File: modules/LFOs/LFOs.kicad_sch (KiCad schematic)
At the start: 12 parts, among them J1 BUS CONNECTOR, J10 LFO3 TRI, J2 LFO1 RMP, J3 LFO1 SQR, J4 LFO1 TRI, J5 LFO2 RMP, J6 LFO2 SQR, J7 LFO2 TRI, J8 LFO3 SAW, J9 LFO3 RMP

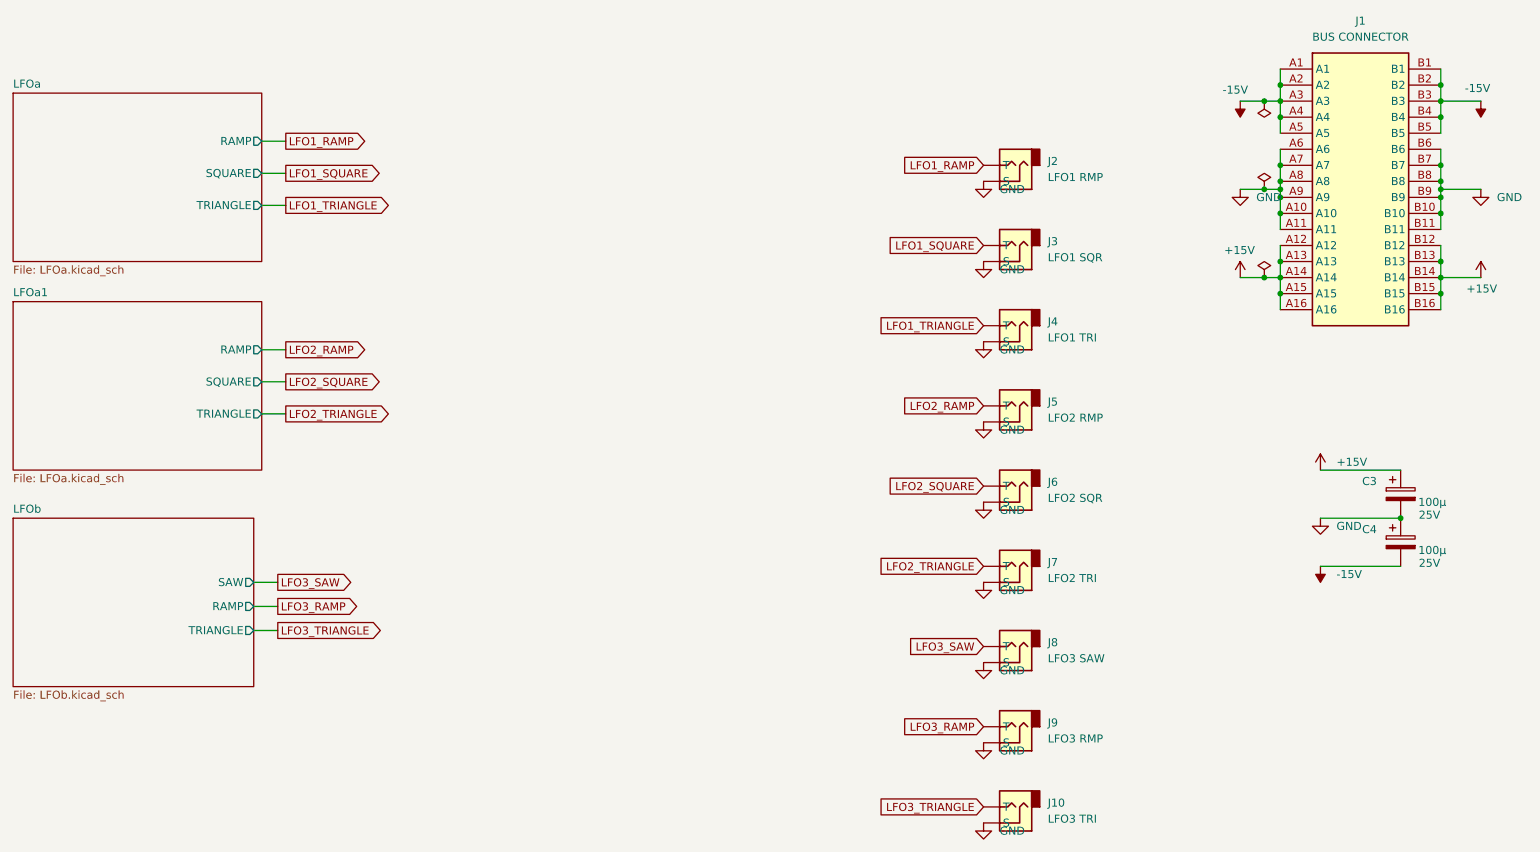
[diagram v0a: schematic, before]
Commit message: lfos overhaul to current template
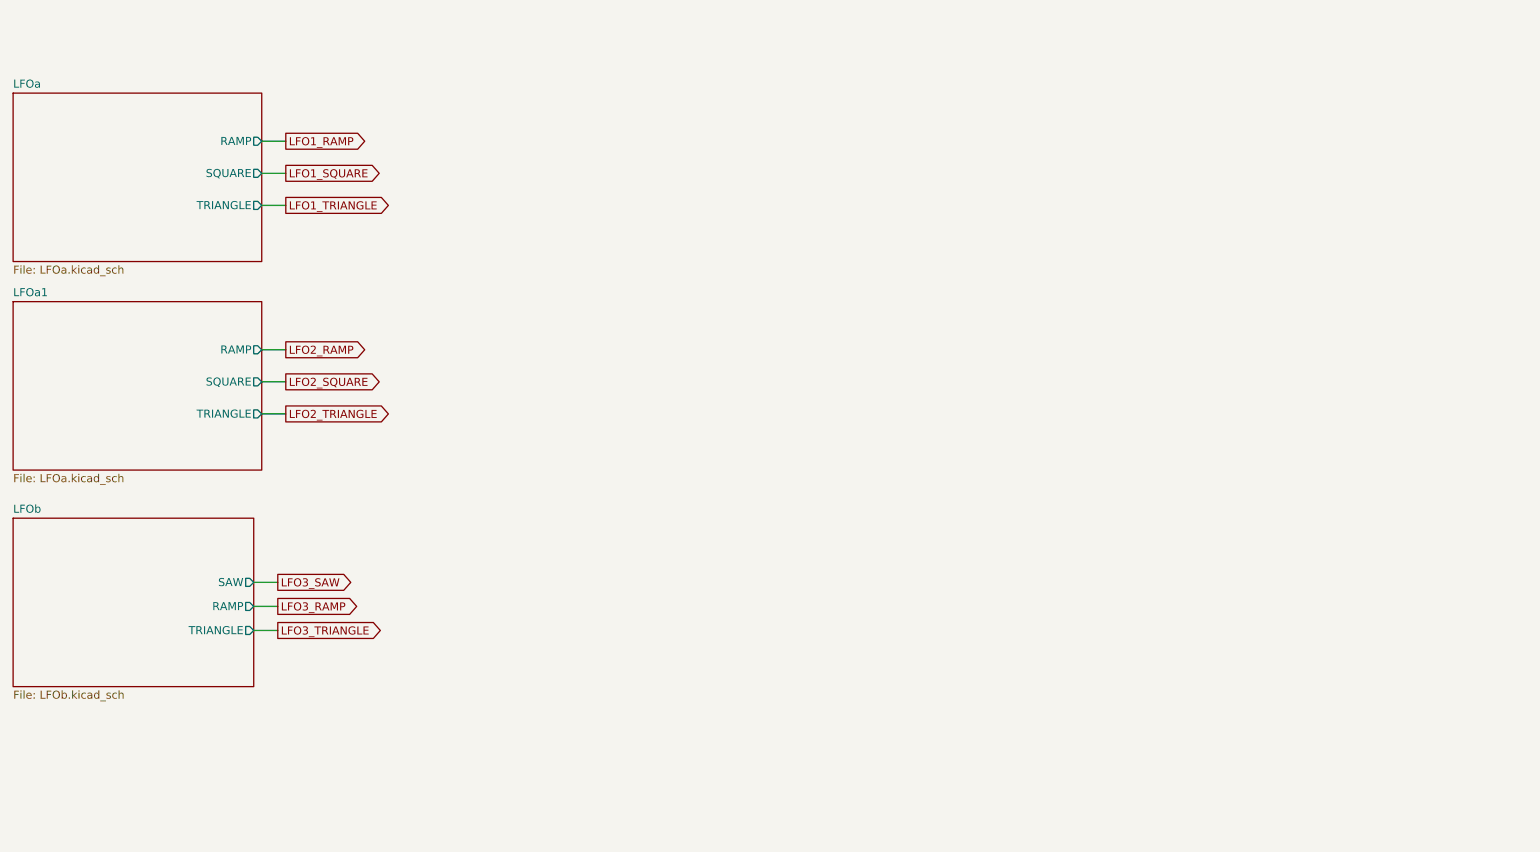
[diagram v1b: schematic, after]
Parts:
- removed C3, C4: 100µ, FormantKO:CP_Axial_800, symbol FormantKO:C_Polarized
- removed J1: BUS CONNECTOR, FormantKO:DIN_Male, symbol FormantKO:DIN_Male
- removed J10: LFO3 TRI, FormantKO:Panel_Connector_1x02, symbol FormantKO:Mono_Jack
- removed J2: LFO1 RMP, FormantKO:Panel_Connector_1x02, symbol FormantKO:Mono_Jack
- removed J3: LFO1 SQR, FormantKO:Panel_Connector_1x02, symbol FormantKO:Mono_Jack
- removed J4: LFO1 TRI, FormantKO:Panel_Connector_1x02, symbol FormantKO:Mono_Jack
- removed J5: LFO2 RMP, FormantKO:Panel_Connector_1x02, symbol FormantKO:Mono_Jack
- removed J6: LFO2 SQR, FormantKO:Panel_Connector_1x02, symbol FormantKO:Mono_Jack
- removed J7: LFO2 TRI, FormantKO:Panel_Connector_1x02, symbol FormantKO:Mono_Jack
- removed J8: LFO3 SAW, FormantKO:Panel_Connector_1x02, symbol FormantKO:Mono_Jack
- removed J9: LFO3 RMP, FormantKO:Panel_Connector_1x02, symbol FormantKO:Mono_Jack
